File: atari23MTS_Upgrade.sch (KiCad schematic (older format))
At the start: 42 parts, among them P1 CONN_01X01, P2 CONN_01X01, P3 CONN_01X01, P4 CONN_01X01, P5 CONN_01X01, P6 CONN_01X01, SW1 SW_PUSH, U1 NCP1117ST33T3G, U2 STM32F401RCTx, U3 74LS138

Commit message: Modified for new MCU
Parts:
- removed C4, C5: C_Small, Capacitors_SMD:C_1206_HandSoldering, symbol C_Small
- removed C6, C7, C8, C9: 100n, Capacitors_SMD:C_1206_HandSoldering, symbol C_Small
- removed D3: ACT, LEDs:LED_1206, symbol Led_Small
- removed R10, R4: 2.2k, Resistors_SMD:R_1206_HandSoldering, symbol R_Small
- removed R5: 220, Resistors_SMD:R_1206_HandSoldering, symbol R_Small
- removed R6, R7, R8, R9: 10K, Resistors_SMD:R_1206_HandSoldering, symbol R_Small
- removed U2: STM32F401RCTx, Housings_QFP:LQFP-64_10x10mm_Pitch0.5mm, symbol STM32F401RCTx
- removed XT1: 8Mhz, Crystals:Crystal_SMD_0603_4Pads, symbol Crystal_Small
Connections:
- net labels added: mA19, mA20, mA21
- net labels removed: PB0, PB1, PB2, PB3, PB4, PB5, PB6, PB7, mA0, mA1, mA2, mA3, mA4, mA5, mA6, mA7, mB02/PHI2, mD0, mD1, mD2, mD3, mD4, mD5, mD6, mD7, mR/~W, ~ADDRSEL16K, ~mCCTL, ~mD1XX, ~mD3XX, ~mEXSEL, ~mHALT, ~mIRQ, ~mMPD, ~mREF, ~mRST
- wire segments 119 -> 31
- no-connect marks 21 -> 13
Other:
- note added: "EXTRA BIT ADDRESS DECODER"
- note removed: "16K BANK SELECTORS"
- note removed: "ADDRESS DECODER"

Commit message: Transformation will begin shortly... ;-)
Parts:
- P2, P3, P4, P5: footprint Connect:1pin -> RetroBitLab:MountingHole
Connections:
- net labels added: mD1E2_A19, mD1E3_A20, mD1E3_A21, ~mD6XX
- net labels removed: mA19, mA20, mA21
- wire segments 31 -> 34
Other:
- note added: "0 0 0"
- note added: "0 0 1"
- note added: "0 1 0"
- note added: "0 1 1"
- note added: "1 0 0"
- note added: "1 0 1"
- note added: "1 1 0"
- note added: "1 1 1"
- note added: "1024k"
- note added: "1536k"
- note added: "2048k"
- note added: "2560k"
- note added: "3072k"
- note added: "3584k"
- note added: "4096k"
- note added: "512k"
- note added: "MEMORY ADDRESS DECODER"
- note added: "mA21 mA20 mA19"
- note added: "mA21 not driving any memory chip yet. Needs more RAM Chips"
- note removed: "EXTRA BIT ADDRESS DECODER"
- moved on the sheet: CART1, DISABLE.MODE.1, ECI1, FT232RPi.1, JP1, P1, R3, STLinkV2.1

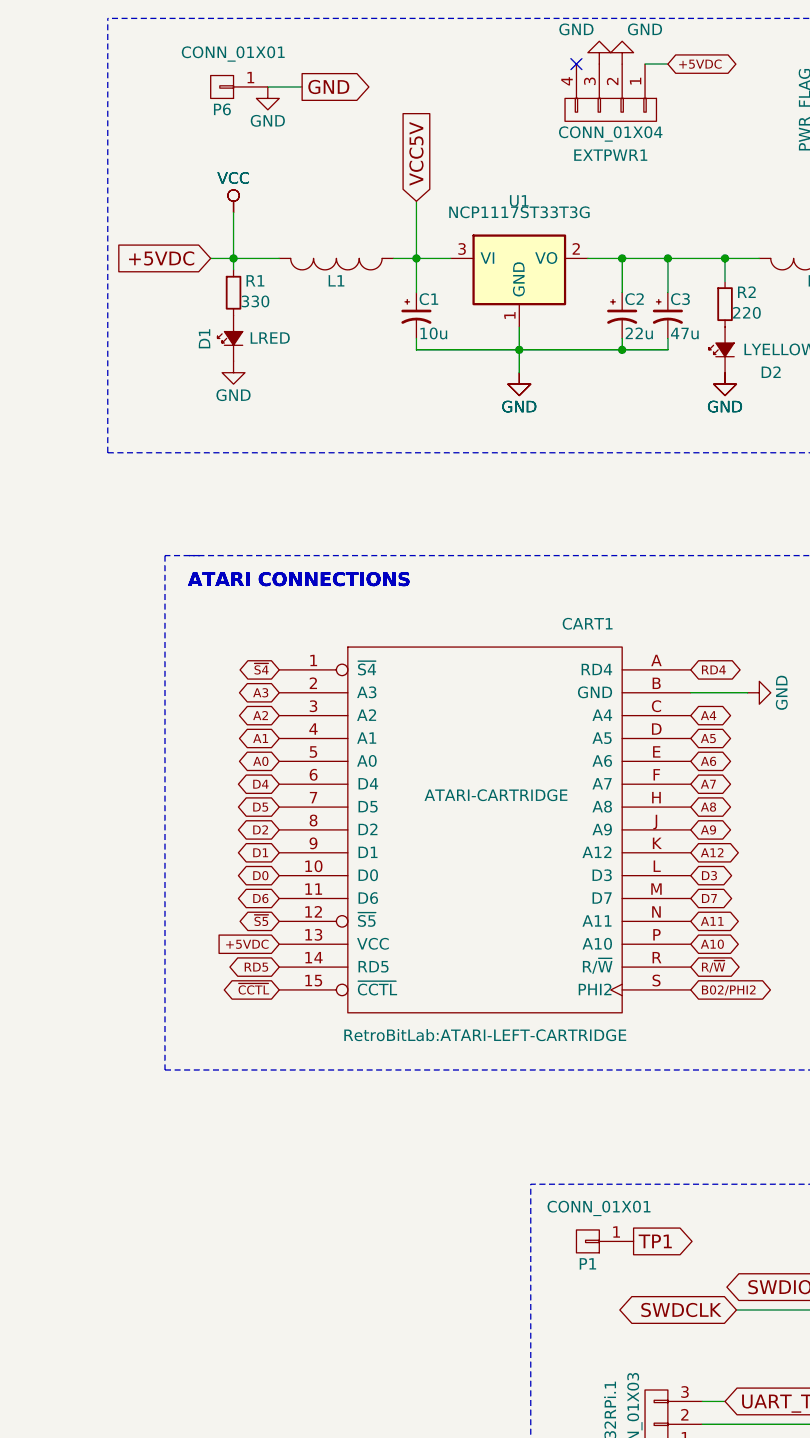
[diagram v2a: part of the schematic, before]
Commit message: Multiple library support for Kicad. Need a reconfiguration at work
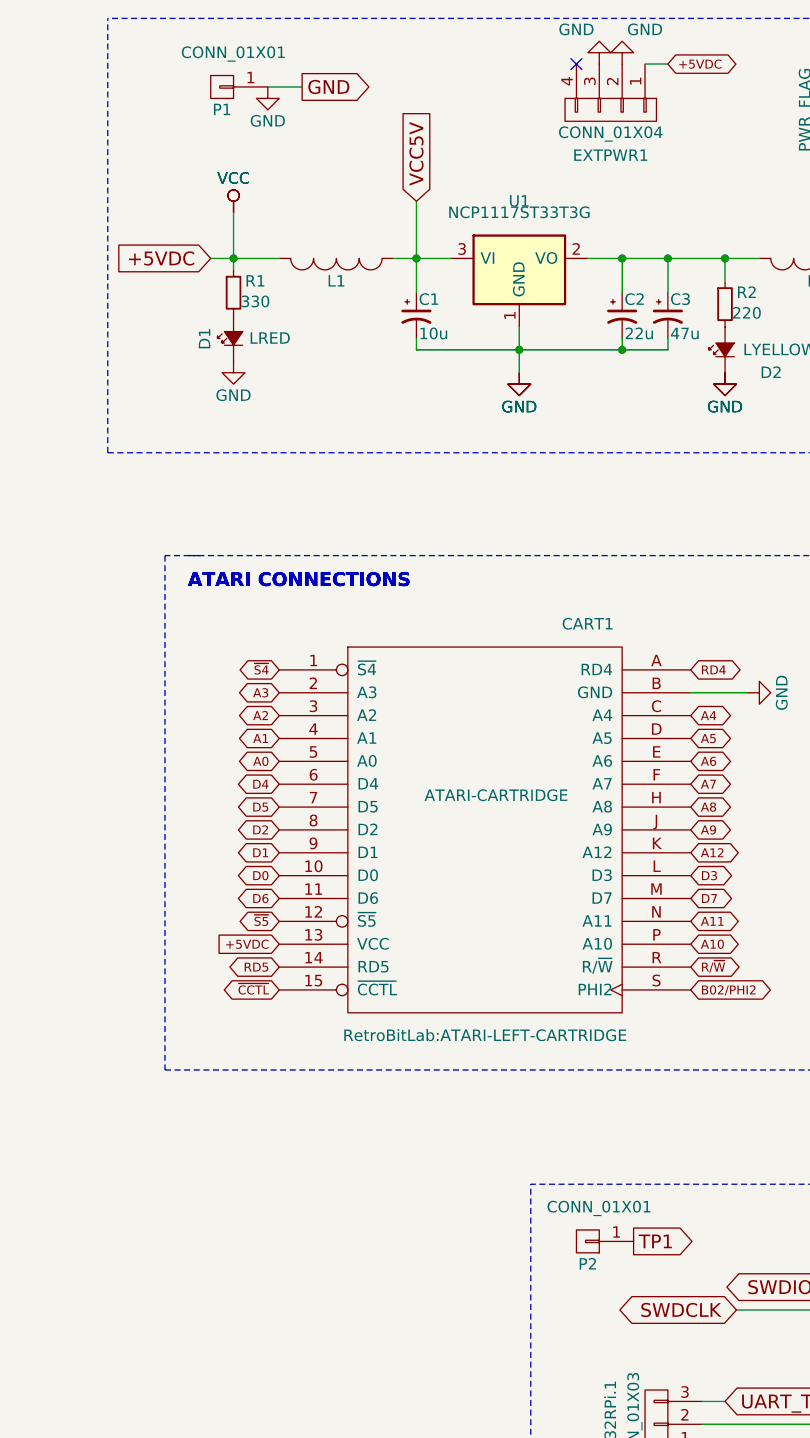
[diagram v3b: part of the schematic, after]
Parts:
- renumbered P6 to P1, P1 to P2, P2 to P3, P3 to P4, P4 to P5, P5 to P6, U3 to U2
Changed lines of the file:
@@
 DEBUG/PROGRAMMING SECTION
 $Comp
-L CONN_01X01 P1
+L CONN_01X01 P2
 U 1 1 5C2B6F21
 P 2650 5900
-F 0 "P1" H 2650 6000 50  0000 C CNN
+F 0 "P2" H 2650 6000 50  0000 C CNN
 F 1 "CONN_01X01" H 2600 5750 50  0000 C CNN
 F 2 "Measurement_Points:Measurement_Point_Round-SMD-Pad_Small" H 2650 5900 50  0001 C CNN
@@
 RESET BUTTON
 $Comp
-L CONN_01X01 P2
+L CONN_01X01 P3
 U 1 1 5C2B6F2C
 P 5350 1550
-F 0 "P2" H 5350 1650 50  0001 C CNN
+F 0 "P3" H 5350 1650 50  0001 C CNN
 F 1 "CONN_01X01" V 5450 1550 50  0001 C CNN
 F 2 "RetroBitLab:MountingHole" V 5550 1550 50  0001 C CNN
@@
 NoConn ~ 5350 1350
 $Comp
-L CONN_01X01 P3
+L CONN_01X01 P4
 U 1 1 5C2B6F2D
 P 5600 1550
-F 0 "P3" H 5600 1650 50  0001 C CNN
+F 0 "P4" H 5600 1650 50  0001 C CNN
 F 1 "CONN_01X01" V 5700 1550 50  0001 C CNN
 F 2 "RetroBitLab:MountingHole" V 5800 1550 50  0001 C CNN
@@
 NoConn ~ 5600 1350
 $Comp
-L CONN_01X01 P4
+L CONN_01X01 P5
 U 1 1 5C2B6F2E
 P 5800 1550
-F 0 "P4" H 5800 1650 50  0001 C CNN
+F 0 "P5" H 5800 1650 50  0001 C CNN
 F 1 "CONN_01X01" V 5900 1550 50  0001 C CNN
 F 2 "RetroBitLab:MountingHole" V 6000 1550 50  0001 C CNN
@@
 NoConn ~ 5800 1350
 $Comp
-L CONN_01X01 P5
+L CONN_01X01 P6
 U 1 1 5C2B6F2F
 P 6050 1550
-F 0 "P5" H 6050 1650 50  0001 C CNN
+F 0 "P6" H 6050 1650 50  0001 C CNN
 F 1 "CONN_01X01" V 6150 1550 50  0001 C CNN
 F 2 "RetroBitLab:MountingHole" V 6250 1550 50  0001 C CNN
@@
 $EndComp
 $Comp
-L 74LS138 U3
+L 74LS138 U2
 U 1 1 5C2F63E8
 P 8750 2150
-F 0 "U3" H 8450 2600 50  0000 C CNN
+F 0 "U2" H 8450 2600 50  0000 C CNN
 F 1 "74LS138" H 8450 1600 50  0000 C CNN
 F 2 "Housings_SSOP:TSSOP-16_4.4x5mm_Pitch0.65mm" H 8750 2150 50  0001 C CNN
@@
 RD5
 $Comp
-L CONN_01X01 P6
+L CONN_01X01 P1
 U 1 1 5C326A2F
 P 1050 850
-F 0 "P6" H 1050 950 50  0000 C CNN
+F 0 "P1" H 1050 950 50  0000 C CNN
 F 1 "CONN_01X01" H 1000 700 50  0000 C CNN
 F 2 "Pin_Headers:Pin_Header_Straight_1x01" H 1050 850 50  0001 C CNN

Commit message: Upgraded with the latest infos
Now there is no logic for address/decoding. All is done inside the
microprocessor. This is a semi-final release.
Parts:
- removed SW1: SW_PUSH, Buttons_Switches_SMD:SW_SPST_FSMSM, symbol SW_PUSH
- removed U2: 74LS138, Housings_SSOP:TSSOP-16_4.4x5mm_Pitch0.65mm, symbol 74LS138
- added SW1: SW_Push, RetroBitLab:SW_SPST_FSMSM_3D, symbol SW_Push
- renumbered P3 to P2, P4 to P3, P5 to P4, P6 to P5, P2 to P6
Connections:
- net labels removed: RAMEN, mD1E2_A19, mD1E3_A20, mD1E3_A21, ~BSEL0, ~BSEL1, ~BSEL2, ~BSEL3, ~mD6XX
- no-connect marks 13 -> 9
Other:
- note removed: "0 0 0"
- note removed: "0 0 1"
- note removed: "0 1 0"
- note removed: "0 1 1"
- note removed: "1 0 0"
- note removed: "1 0 1"
- note removed: "1 1 0"
- note removed: "1 1 1"
- note removed: "1024k"
- note removed: "1536k"
- note removed: "2048k"
- note removed: "2560k"
- note removed: "3072k"
- note removed: "3584k"
- note removed: "4096k"
- note removed: "512k"
- note removed: "MEMORY ADDRESS DECODER"
- note removed: "mA21 mA20 mA19"
- note removed: "mA21 not driving any memory chip yet. Needs more RAM Chips"
- moved on the sheet: DISABLE.MODE.1, FT232RPi.1, JP1, P6, R3, STLinkV2.1

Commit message: Modified for dual processors board
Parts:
- added DISABLE.MODE.2: CONN_01X02, Pin_Headers:Pin_Header_Straight_1x02, symbol CONN_01X02
- added JP2: CONN_01X03, Pin_Headers:Pin_Header_Straight_1x03, symbol CONN_01X03
- added R4: 10K, Resistors_SMD:R_1206_HandSoldering, symbol R_Small
- added STLinkV2.1: CONN_01X04, Pin_Headers:Pin_Header_Angled_1x04, symbol CONN_01X04
- added SW2: SW_Push, RetroBitLab:SW_SPST_FSMSM_3D, symbol SW_Push
- renumbered R3 to R2, R2 to R3, STLinkV2.1 to STLinkV2.2
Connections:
- net GND: now also DISABLE.MODE.2.2 (P2), JP2.3 (P3), STLinkV2.1.1 (P1), SW2.1
- net VCC3V3: now also JP2.1 (P1), R4.2, STLinkV2.1.4 (P4)
- net BOOT0 renamed BOOT0_CART
- net SWDCLK renamed SWDCLK_MEM
- net SWDIO renamed SWDIO_MEM
- net UART_RX_TTL renamed UART_RX
- net UART_TX_TTL renamed UART_TX
- net nRESET renamed nRESET_CART
- new net BOOT0_MEM: JP2.2 (P2)
- new net SWDCLK_CART: STLinkV2.1.3 (P3)
- new net SWDIO_CART: STLinkV2.1.2 (P2)
- new net nRESET_MEM: DISABLE.MODE.2.1 (P1), R4.1, SW2.2
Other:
- note added: "BOOTSEL CART"
- note added: "BOOTSEL MEM"
- note added: "DEBUG/PROGRAMMING SECTION CART"
- note added: "DEBUG/PROGRAMMING SECTION MEMORY"
- note added: "RESET BUTTON CART"
- note added: "RESET BUTTON MEM"
- note removed: "BOOTSEL"
- note removed: "DEBUG/PROGRAMMING SECTION"
- note removed: "RESET BUTTON"
- moved on the sheet: DISABLE.MODE.1, FT232RPi.1, JP1, P6, R2, STLinkV2.2, SW1

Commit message: C64 Emulation. First run on my beloved ATARI 130XE.
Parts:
- C1, C2, C3: footprint Capacitors_SMD:c_elec_5x5.3 -> Capacitor_SMD:CP_Elec_5x5.3; symbol CP1_Small -> Device1:CP1_Small
- CART1: symbol ATARICARTRIDGE -> AmigaComponents:ATARICARTRIDGE
- D1, D2: footprint LEDs:LED_1206 -> LED_SMD:LED_1206_3216Metric_Pad1.42x1.75mm_HandSolder; symbol Led_Small -> atari23MTS_Upgrade-rescue:Led_Small
- DISABLE.MODE.1, DISABLE.MODE.2: footprint Pin_Headers:Pin_Header_Straight_1x02 -> Connector_PinHeader_2.54mm:PinHeader_1x02_P2.54mm_Vertical; symbol CONN_01X02 -> atari23MTS_Upgrade-rescue:CONN_01X02
- ECI1: symbol ECIBUS -> AmigaComponents:ECIBUS
- EXTPWR1, STLinkV2.1, STLinkV2.2: footprint Pin_Headers:Pin_Header_Angled_1x04 -> Connector_PinHeader_2.54mm:PinHeader_1x04_P2.54mm_Horizontal; symbol CONN_01X04 -> atari23MTS_Upgrade-rescue:CONN_01X04
- FT232RPi.1, JP1, JP2: footprint Pin_Headers:Pin_Header_Straight_1x03 -> Connector_PinHeader_2.54mm:PinHeader_1x03_P2.54mm_Vertical; symbol CONN_01X03 -> atari23MTS_Upgrade-rescue:CONN_01X03
- L1, L2: footprint Choke_SMD:Choke_SMD_1206_Handsoldering -> Inductor_SMD:L_1206_3216Metric_Pad1.42x1.75mm_HandSolder; symbol INDUCTOR_SMALL -> atari23MTS_Upgrade-rescue:INDUCTOR_SMALL
- P1: footprint Pin_Headers:Pin_Header_Straight_1x01 -> Connector_PinHeader_2.54mm:PinHeader_1x01_P2.54mm_Vertical; symbol CONN_01X01 -> atari23MTS_Upgrade-rescue:CONN_01X01
- P2, P3, P4, P5: symbol CONN_01X01 -> atari23MTS_Upgrade-rescue:CONN_01X01
- P6: footprint Measurement_Points:Measurement_Point_Round-SMD-Pad_Small -> TestPoint:TestPoint_Pad_D2.0mm; symbol CONN_01X01 -> atari23MTS_Upgrade-rescue:CONN_01X01
- R1, R2, R3, R4: footprint Resistors_SMD:R_1206_HandSoldering -> Resistor_SMD:R_1206_3216Metric_Pad1.42x1.75mm_HandSolder; symbol R_Small -> Device1:R_Small
- SW1, SW2: symbol SW_Push -> Switch1:SW_Push
- U1: footprint TO_SOT_Packages_SMD:SOT-223 -> Package_TO_SOT_SMD:SOT-223; symbol NCP1117ST33T3G-RESCUE-atari23MTS_Upgrade -> atari23MTS_Upgrade-rescue:NCP1117ST33T3G-RESCUE-atari23MTS_Upgrade
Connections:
- no-connect marks 9 -> 5

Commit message: RetroBitLab library
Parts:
- CART1: symbol AmigaComponents:ATARICARTRIDGE -> RetroBitLab:ATARICARTRIDGE
- ECI1: symbol AmigaComponents:ECIBUS -> RetroBitLab:ECIBUS
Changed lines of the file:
@@
 TP1
 $Comp
-L AmigaComponents:ATARICARTRIDGE CART1
+L RetroBitLab:ATARICARTRIDGE CART1
 U 1 1 5C2B6F23
 P 2200 4050
@@
 $EndComp
 $Comp
-L AmigaComponents:ECIBUS ECI1
+L RetroBitLab:ECIBUS ECI1
 U 1 1 5C2B6F24
 P 5350 4000
